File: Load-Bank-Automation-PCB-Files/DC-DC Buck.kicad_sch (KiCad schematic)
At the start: 28 parts, among them Q1 NMOS, Q2 NMOS, U1 LM25145RGYT

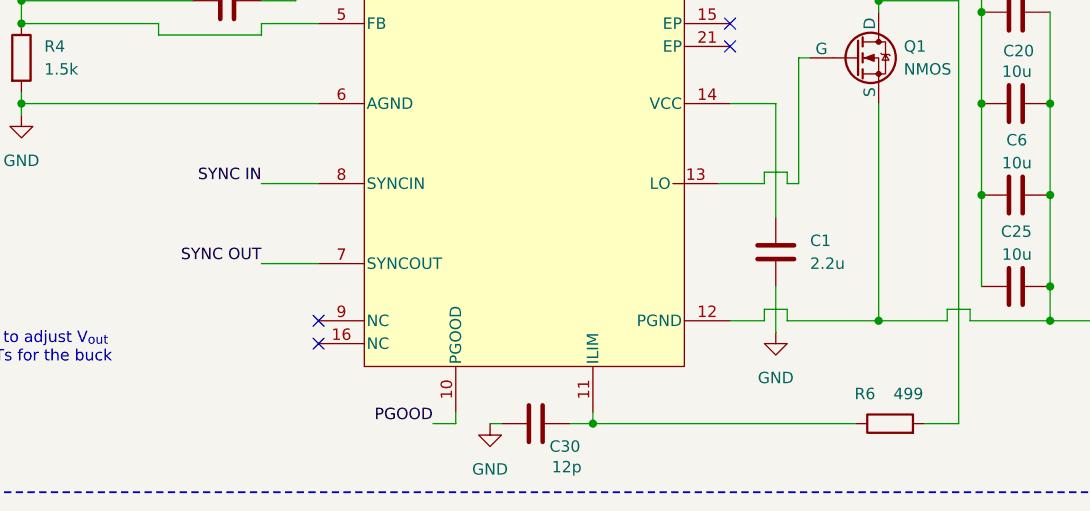
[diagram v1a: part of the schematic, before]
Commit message: Completed eFuse and Starting on Layout
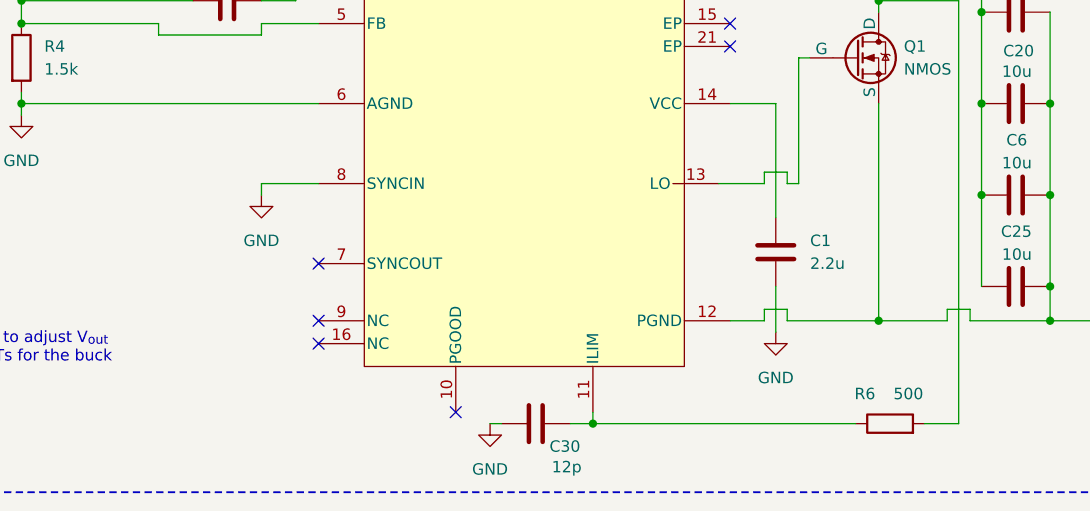
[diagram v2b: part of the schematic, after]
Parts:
- C1, C10, C2, C20, C25, C26, C27, C28, C29, C3, C30, C31, C4, C6, C7, C8, L1, R11, R12, R4, R5, R7, R8, R9: footprint (none) -> Resistor_SMD:R_0603_1608Metric
- R6: value 499 -> 500; footprint (none) -> Resistor_SMD:R_0603_1608Metric
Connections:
- net SYNC IN is gone; now on net GND: U1.8 (SYNCIN)
- net PGOOD: no longer names the net of U1.10 (PGOOD)
- net SYNC OUT: no longer names the net of U1.7 (SYNCOUT)
- no-connect marks 4 -> 6
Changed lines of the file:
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@@
 	)
 	(no_connect
+		(at 121.92 114.3)
+	)
+	(no_connect
 		(at 121.92 120.65)
 	)
@@
 		(at 167.64 90.17)
 	)
-	(wire
-		(pts
-			(xy 137.16 132.08) (xy 134.62 132.08)
-		)
-		(stroke
-			(width 0)
-			(type default)
-		)
+	(no_connect
+		(at 137.16 130.81)
 	)
 	(wire
@@
 	(wire
 		(pts
-			(xy 115.57 114.3) (xy 121.92 114.3)
-		)
-		(stroke
-			(width 0)
-			(type default)
-		)
-	)
-	(wire
-		(pts
 			(xy 182.88 77.47) (xy 185.42 77.47)
 		)
@@
 	(wire
 		(pts
+			(xy 115.57 105.41) (xy 115.57 106.68)
+		)
+		(stroke
+			(width 0)
+			(type default)
+		)
+	)
+	(wire
+		(pts
 			(xy 82.55 72.39) (xy 82.55 71.12)
 		)
@@
 	(wire
 		(pts
-			(xy 137.16 130.81) (xy 137.16 132.08)
-		)
-		(stroke
-			(width 0)
-			(type default)
-		)
-	)
-	(wire
-		(pts
 			(xy 173.99 104.14) (xy 173.99 105.41)
 		)
@@
 		)
 	)
-	(label "SYNC IN"
-		(at 115.57 105.41 180)
-		(effects
-			(font
-				(size 1.27 1.27)
-			)
-			(justify right bottom)
-		)
-	)
-	(label "PGOOD"
-		(at 134.62 132.08 180)
-		(effects
-			(font
-				(size 1.27 1.27)
-			)
-			(justify right bottom)
-		)
-	)
-	(label "SYNC OUT"
-		(at 115.57 114.3 180)
-		(effects
-			(font
-				(size 1.27 1.27)
-			)
-			(justify right bottom)
-		)
-	)
 	(hierarchical_label "(14.4<V<36)_{in}"
 		(shape input)
@@
 			)
 		)
-		(property "Footprint" ""
+		(property "Footprint" "Resistor_SMD:R_0603_1608Metric"
 			(at 203.2 115.8748 0)
 			(effects
@@
 			)
 		)
-		(property "Footprint" ""
+		(property "Footprint" "Resistor_SMD:R_0603_1608Metric"
 			(at 173.6852 68.58 0)
 			(effects
@@
 			)
 		)
-		(property "Footprint" ""
+		(property "Footprint" "Resistor_SMD:R_0603_1608Metric"
 			(at 115.57 77.7748 0)
 			(effects
@@
 			)
 		)
-		(property "Footprint" ""
+		(property "Footprint" "Resistor_SMD:R_0603_1608Metric"
 			(at 140.97 49.2252 0)
 			(effects
@@
 			)
 		)
-		(property "Footprint" ""
+		(property "Footprint" "Resistor_SMD:R_0603_1608Metric"
 			(at 109.22 59.182 90)
 			(effects
@@
 			)
 		)
-		(property "Value" "499"
+		(property "Value" "500"
 			(at 187.452 128.778 90)
 			(effects
@@
 			)
 		)
-		(property "Footprint" ""
+		(property "Footprint" "Resistor_SMD:R_0603_1608Metric"
 			(at 185.42 133.858 90)
 			(effects
@@
 			)
 		)
-		(property "Footprint" ""
+		(property "Footprint" "Resistor_SMD:R_0603_1608Metric"
 			(at 101.6 80.518 90)
 			(effects
@@
 			)
 		)
-		(property "Footprint" ""
+		(property "Footprint" "Resistor_SMD:R_0603_1608Metric"
 			(at 218.44 85.3948 0)
 			(effects
@@
 			)
 		)
-		(property "Footprint" ""
+		(property "Footprint" "Resistor_SMD:R_0603_1608Metric"
 			(at 87.122 91.44 90)
 			(effects
@@
 			)
 		)
-		(property "Footprint" ""
+		(property "Footprint" "Resistor_SMD:R_0603_1608Metric"
 			(at 218.44 105.7148 0)
 			(effects
@@
 			)
 		)
-		(property "Footprint" ""
+		(property "Footprint" "Resistor_SMD:R_0603_1608Metric"
 			(at 120.65 70.8152 0)
 			(effects
@@
 			)
 		)
-		(property "Footprint" ""
+		(property "Footprint" "Resistor_SMD:R_0603_1608Metric"
 			(at 218.44 115.8748 0)
 			(effects
@@
 			)
 		)
-		(property "Footprint" ""
+		(property "Footprint" "Resistor_SMD:R_0603_1608Metric"
 			(at 173.6852 116.84 0)
 			(effects
@@
 			)
 		)
-		(property "Footprint" ""
+		(property "Footprint" "Resistor_SMD:R_0603_1608Metric"
 			(at 218.44 95.5548 0)
 			(effects
@@
 			)
 		)
-		(property "Footprint" ""
+		(property "Footprint" "Resistor_SMD:R_0603_1608Metric"
 			(at 203.2 105.7148 0)
 			(effects
@@
 			)
 		)
-		(property "Footprint" ""
+		(property "Footprint" "Resistor_SMD:R_0603_1608Metric"
 			(at 81.5848 71.12 0)
 			(effects
@@
 			)
 		)
-		(property "Footprint" ""
+		(property "Footprint" "Resistor_SMD:R_0603_1608Metric"
 			(at 144.78 42.418 90)
 			(effects
@@
 	)
 	(symbol
+		(lib_id "power:GND")
+		(at 115.57 106.68 0)
+		(unit 1)
+		(exclude_from_sim no)
+		(in_bom yes)
+		(on_board yes)
+		(dnp no)
+		(fields_autoplaced yes)
+		(property "Reference" "#PWR0101"
+			(at 115.57 113.03 0)
+			(effects
+				(font
+					(size 1.27 1.27)
+				)
+				(hide yes)
+			)
+		)
+		(property "Value" "GND"
+			(at 115.57 111.76 0)
+			(effects
+				(font
+					(size 1.27 1.27)
+				)
+			)
+		)
+		(property "Footprint" ""
+			(at 115.57 106.68 0)
+			(effects
+				(font
+					(size 1.27 1.27)
+				)
+				(hide yes)
+			)
+		)
+		(property "Datasheet" ""
+			(at 115.57 106.68 0)
+			(effects
+				(font
+					(size 1.27 1.27)
+				)
+				(hide yes)
+			)
+		)
+		(property "Description" "Power symbol creates a global label with name \"GND\" , ground"
+			(at 115.57 106.68 0)
+			(effects
+				(font
+					(size 1.27 1.27)
+				)
+				(hide yes)
+			)
+		)
+		(pin "1"
+		)
+		(instances
+			(project ""
+				(path "/c82c4769-33eb-46b7-8d07-39045014a3da/eb9b9647-818b-4f6a-aec9-7481a1a3b43c/36fe7d56-cf73-41f9-a092-e3a444c4baa1"
+					(reference "#PWR0101")
+					(unit 1)
+				)
+			)
+		)
+	)
+	(symbol
 		(lib_id "Device:R")
 		(at 130.81 40.64 90)
@@
 			)
 		)
-		(property "Footprint" ""
+		(property "Footprint" "Resistor_SMD:R_0603_1608Metric"
 			(at 130.81 42.418 90)
 			(effects
@@
 			)
 		)
-		(property "Footprint" ""
+		(property "Footprint" "Resistor_SMD:R_0603_1608Metric"
 			(at 115.57 84.1248 0)
 			(effects
@@
 			)
 		)
-		(property "Footprint" ""
+		(property "Footprint" "Resistor_SMD:R_0603_1608Metric"
 			(at 203.2 85.3948 0)
 			(effects
@@
 			)
 		)
-		(property "Footprint" ""
+		(property "Footprint" "Resistor_SMD:R_0603_1608Metric"
 			(at 84.328 58.42 90)
 			(effects
@@
 			)
 		)
-		(property "Footprint" ""
+		(property "Footprint" "Resistor_SMD:R_0603_1608Metric"
 			(at 87.122 58.42 90)
 			(effects
@@
 			)
 		)
-		(property "Footprint" ""
+		(property "Footprint" "Resistor_SMD:R_0603_1608Metric"
 			(at 203.2 95.5548 0)
 			(effects
@@
 			)
 		)
-		(property "Footprint" ""
+		(property "Footprint" "Resistor_SMD:R_0603_1608Metric"
 			(at 149.86 131.1148 0)
 			(effects
@@
 			)
 		)
-		(property "Footprint" ""
+		(property "Footprint" "Resistor_SMD:R_0603_1608Metric"
 			(at 213.36 78.74 0)
 			(effects

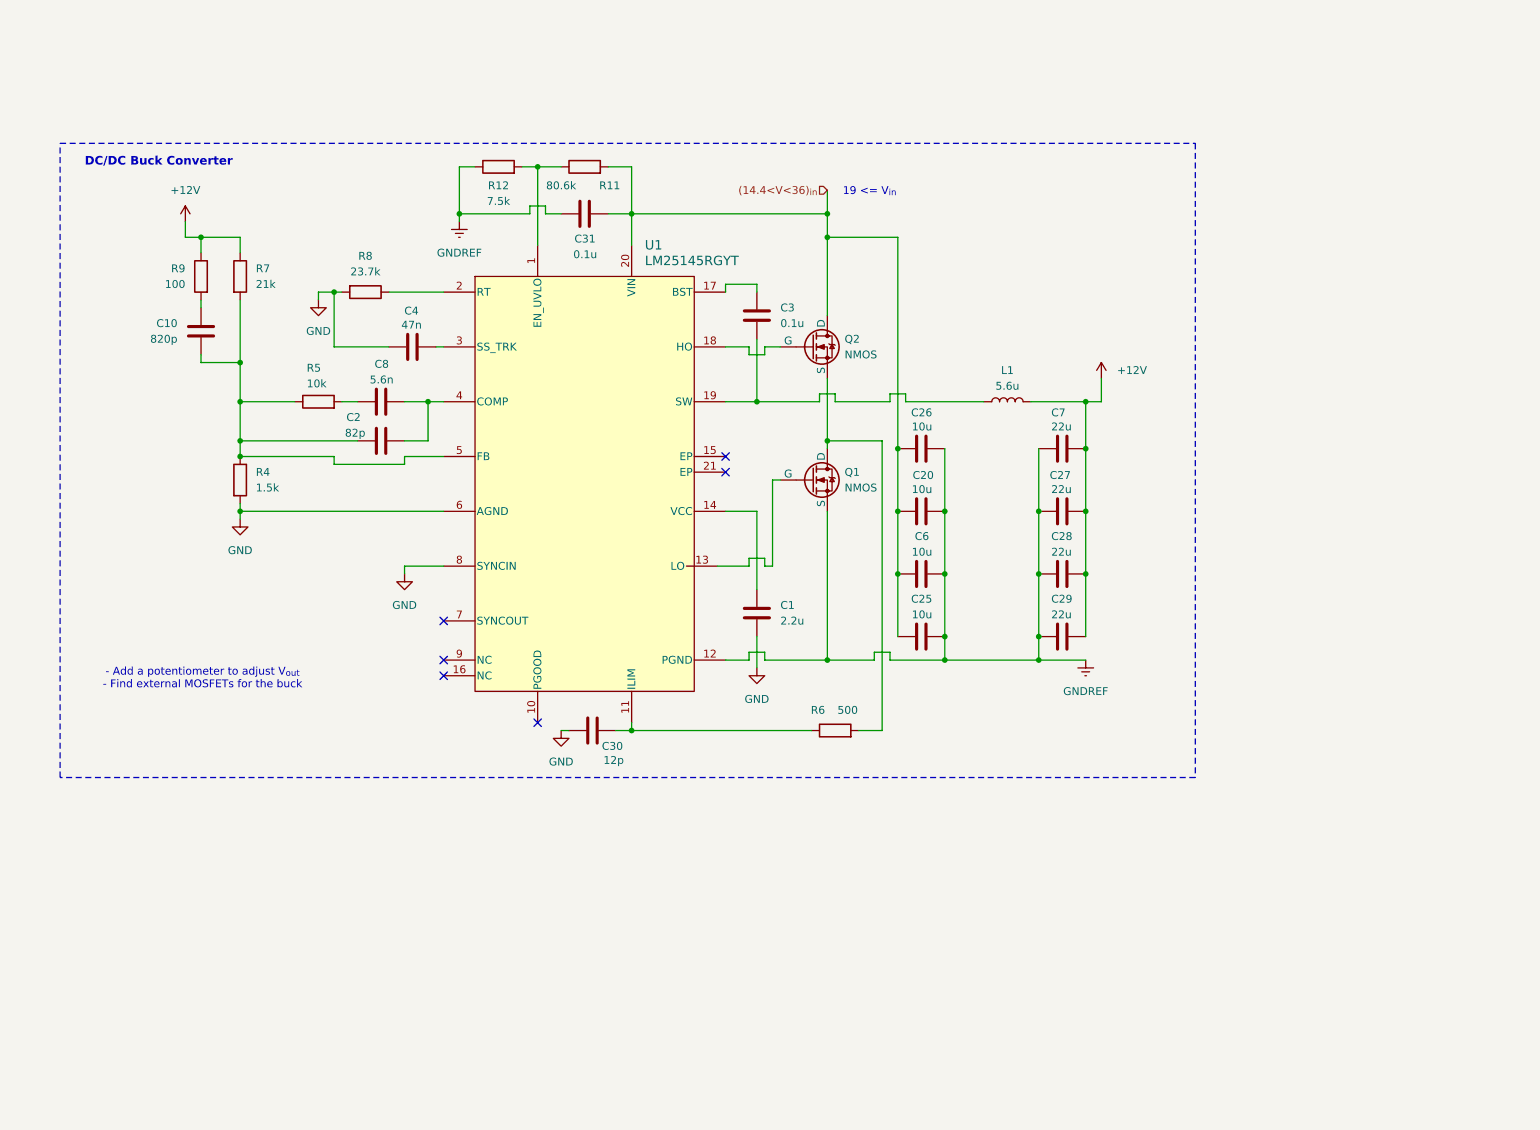
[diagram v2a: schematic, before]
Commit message: New MCU, Configured Pins, Attached some footprints
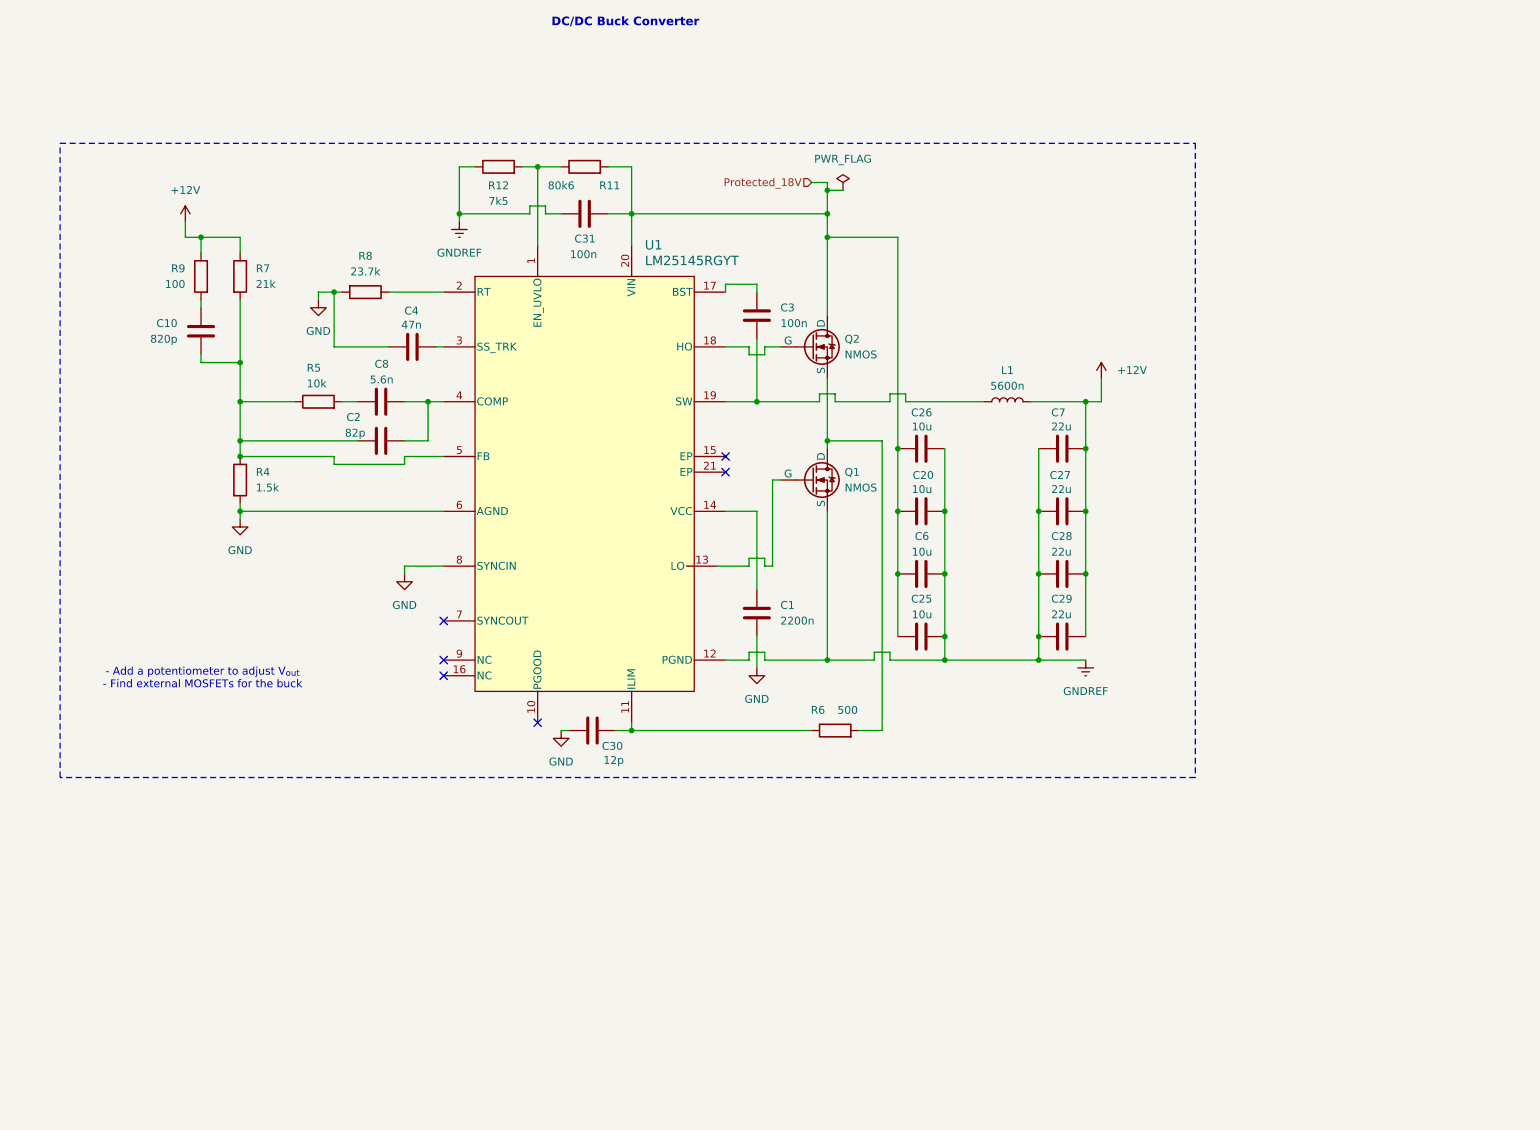
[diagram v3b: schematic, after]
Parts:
- C1: value 2.2u -> 2200n
- C3, C31: value 0.1u -> 100n
- L1: value 5.6u -> 5600n
- R11: value 80.6k -> 80k6
- R12: value 7.5k -> 7k5
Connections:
- net (14.4<V<36)_{in} renamed Protected_18V
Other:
- note removed: "19 <= V_{in}"
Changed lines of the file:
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@@
 	(text "DC/DC Buck Converter "
 		(exclude_from_sim no)
-		(at 75.692 39.878 0)
+		(at 151.384 17.272 0)
 		(effects
 			(font
@@
 		)
 	)
-	(text "19 <= V_{in}"
-		(exclude_from_sim no)
-		(at 191.008 44.704 0)
-		(effects
-			(font
-				(size 1.27 1.27)
-			)
-		)
-	)
 	(text "- Add a potentiometer to adjust V_{out}\n- Find external MOSFETs for the buck"
 		(exclude_from_sim no)
@@
 	)
 	(junction
-		(at 184.15 48.26)
-		(diameter 0)
-		(color 0 0 0 0)
-	)
-	(junction
 		(at 218.44 96.52)
 		(diameter 0)
@@
 	)
 	(junction
+		(at 184.15 48.26)
+		(diameter 0)
+		(color 0 0 0 0)
+	)
+	(junction
 		(at 152.4 132.08)
 		(diameter 0)
@@
 	)
 	(junction
+		(at 184.15 44.45)
+		(diameter 0)
+		(color 0 0 0 0)
+	)
+	(junction
 		(at 137.16 40.64)
 		(diameter 0)
@@
 	(wire
 		(pts
+			(xy 181.61 43.18) (xy 184.15 43.18)
+		)
+		(stroke
+			(width 0)
+			(type default)
+		)
+	)
+	(wire
+		(pts
 			(xy 88.9 96.52) (xy 121.92 96.52)
 		)
@@
 	(wire
 		(pts
+			(xy 184.15 44.45) (xy 184.15 43.18)
+		)
+		(stroke
+			(width 0)
+			(type default)
+		)
+	)
+	(wire
+		(pts
 			(xy 184.15 74.93) (xy 184.15 85.09)
 		)
@@
 	(wire
 		(pts
+			(xy 184.15 48.26) (xy 184.15 44.45)
+		)
+		(stroke
+			(width 0)
+			(type default)
+		)
+	)
+	(wire
+		(pts
 			(xy 82.55 72.39) (xy 82.55 71.12)
 		)
@@
 	(wire
 		(pts
+			(xy 184.15 44.45) (xy 186.69 44.45)
+		)
+		(stroke
+			(width 0)
+			(type default)
+		)
+	)
+	(wire
+		(pts
 			(xy 88.9 85.09) (xy 88.9 87.63)
 		)
@@
 	(wire
 		(pts
-			(xy 184.15 44.45) (xy 184.15 48.26)
-		)
-		(stroke
-			(width 0)
-			(type default)
-		)
-	)
-	(wire
-		(pts
 			(xy 171.45 119.38) (xy 173.99 119.38)
 		)
@@
 		)
 	)
-	(hierarchical_label "(14.4<V<36)_{in}"
+	(hierarchical_label "Protected_18V"
 		(shape input)
-		(at 184.15 44.45 180)
+		(at 181.61 43.18 180)
 		(effects
 			(font
@@
 			)
 		)
-		(property "Value" "0.1u"
+		(property "Value" "100n"
 			(at 176.53 66.0399 0)
 			(effects
@@
 			)
 		)
-		(property "Value" "0.1u"
+		(property "Value" "100n"
 			(at 146.812 54.864 90)
 			(effects
@@
 			)
 		)
-		(property "Value" "2.2u"
+		(property "Value" "2200n"
 			(at 176.53 114.2999 0)
 			(effects
@@
 			)
 		)
-		(property "Value" "80.6k"
+		(property "Value" "80k6"
 			(at 140.97 43.688 90)
 			(effects
@@
 			)
 		)
-		(property "Value" "7.5k"
+		(property "Value" "7k5"
 			(at 130.81 46.228 90)
 			(effects
@@
 	)
 	(symbol
+		(lib_id "power:PWR_FLAG")
+		(at 186.69 44.45 0)
+		(unit 1)
+		(exclude_from_sim no)
+		(in_bom yes)
+		(on_board yes)
+		(dnp no)
+		(fields_autoplaced yes)
+		(property "Reference" "#FLG03"
+			(at 186.69 42.545 0)
+			(effects
+				(font
+					(size 1.27 1.27)
+				)
+				(hide yes)
+			)
+		)
+		(property "Value" "PWR_FLAG"
+			(at 186.69 39.37 0)
+			(effects
+				(font
+					(size 1.27 1.27)
+				)
+			)
+		)
+		(property "Footprint" ""
+			(at 186.69 44.45 0)
+			(effects
+				(font
+					(size 1.27 1.27)
+				)
+				(hide yes)
+			)
+		)
+		(property "Datasheet" "~"
+			(at 186.69 44.45 0)
+			(effects
+				(font
+					(size 1.27 1.27)
+				)
+				(hide yes)
+			)
+		)
+		(property "Description" "Special symbol for telling ERC where power comes from"
+			(at 186.69 44.45 0)
+			(effects
+				(font
+					(size 1.27 1.27)
+				)
+				(hide yes)
+			)
+		)
+		(pin "1"
+		)
+		(instances
+			(project "Main Board"
+				(path "/c82c4769-33eb-46b7-8d07-39045014a3da/eb9b9647-818b-4f6a-aec9-7481a1a3b43c/36fe7d56-cf73-41f9-a092-e3a444c4baa1"
+					(reference "#FLG03")
+					(unit 1)
+				)
+			)
+		)
+	)
+	(symbol
 		(lib_id "Device:L")
 		(at 213.36 78.74 90)
@@
 			)
 		)
-		(property "Value" "5.6u"
+		(property "Value" "5600n"
 			(at 213.36 76.2 90)
 			(effects
